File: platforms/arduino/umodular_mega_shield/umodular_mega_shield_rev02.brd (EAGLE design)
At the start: 53.5 x 100.1 mm, 31 parts, among them IC1 23LC1024, IC2 74HC4050/CD4050, IC3 6N138, U1 ARDUINO-MEGA-SHIELD

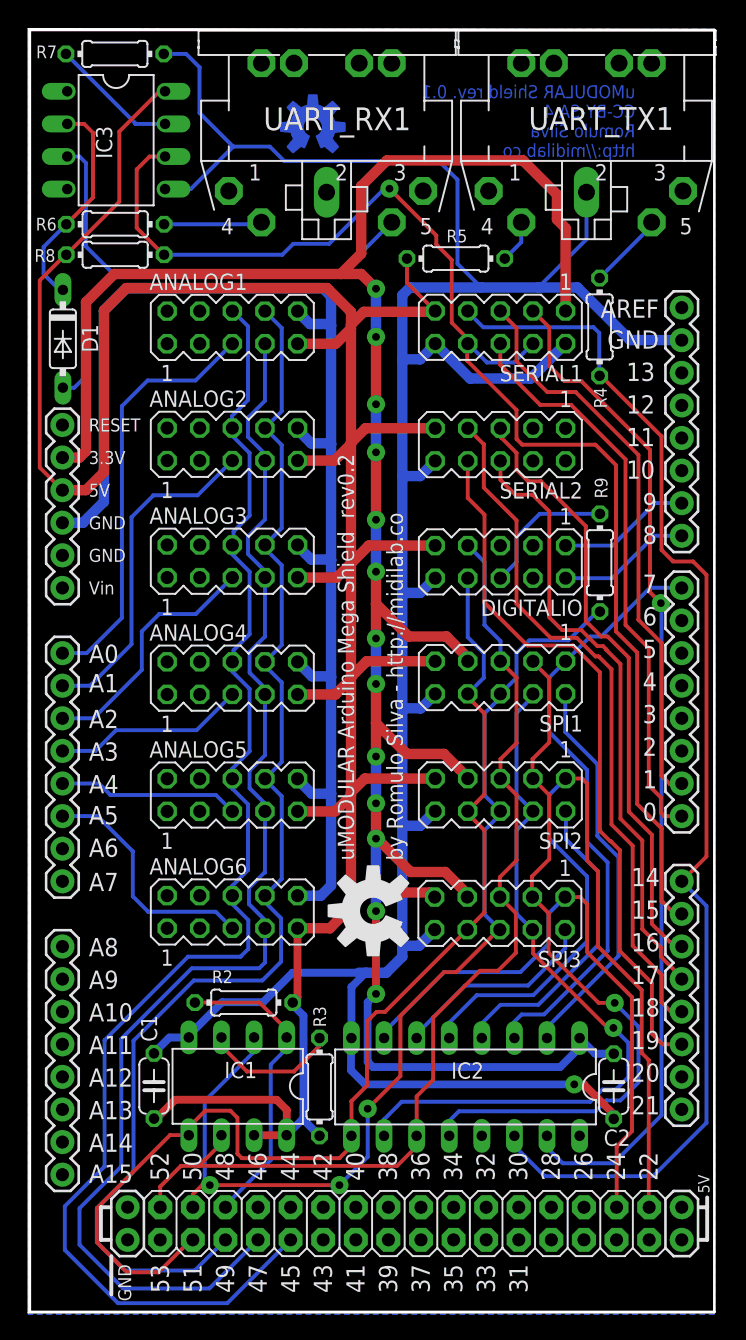
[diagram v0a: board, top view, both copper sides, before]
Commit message: added platform arduino mega shiled a external power connector.
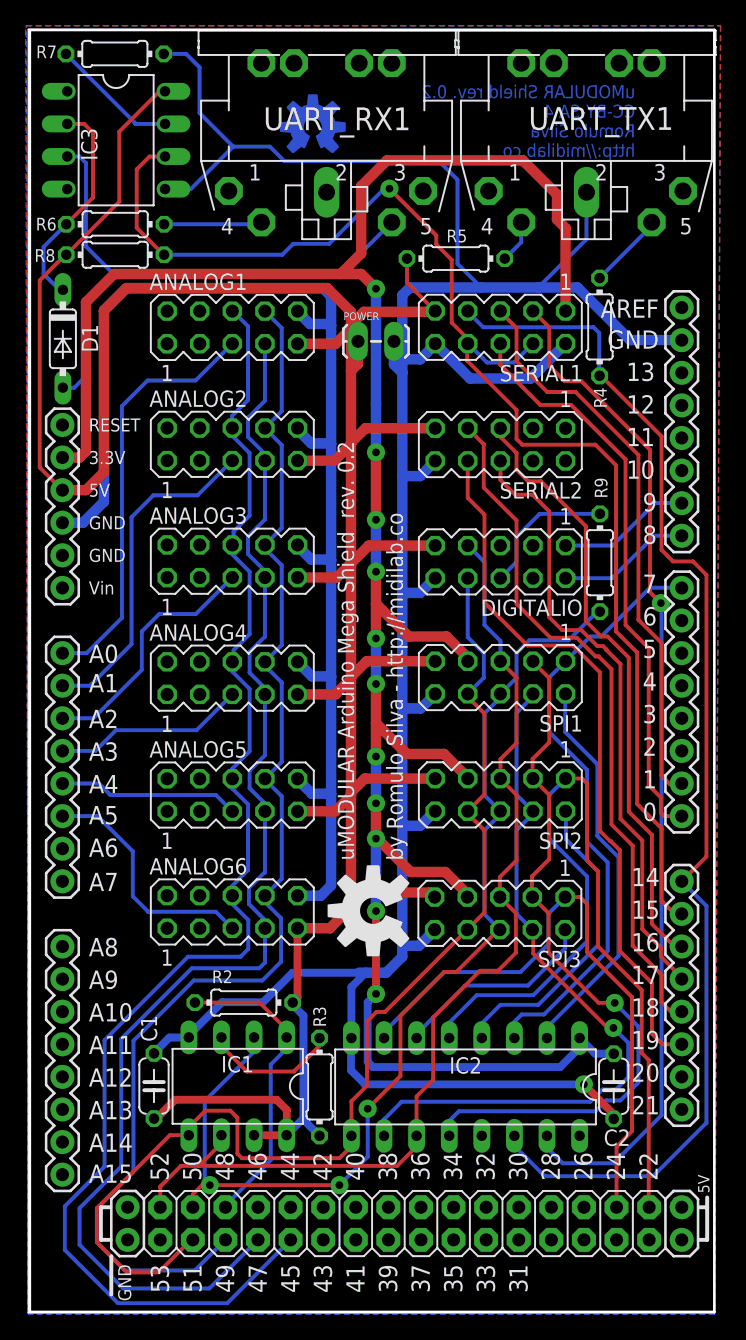
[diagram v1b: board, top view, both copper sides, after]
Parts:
- added POWER: +5V, SparkFun-Connectors:1X02_LOCK_LONGPADS
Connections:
- net GND: now also POWER.2
- net VCC: now also POWER.1
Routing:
- net GND: track 213.0 -> 215.7 mm
- net VCC: track 230.1 -> 232.6 mm
- net VCC_3_3V: vias 13 -> 11
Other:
- board size 53.5 x 100.1 mm -> 53.5 x 100 mm
- board text added: "uMODULAR Arduino Mega Shield rev. 0.2 by Romulo Silva - http://midilab.co"
- board text added: "uMODULAR Shield rev. 0.2 CC-BY-SA 4 Romulo Silva http://midilab.co"
- board text removed: "uMODULAR Arduino Mega Shield rev0.2 by Romulo Silva - http://midilab.co"
- board text removed: "uMODULAR Shield rev. 0.1 CC-BY-SA 4 Romulo Silva http://midilab.co"
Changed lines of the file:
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@@
 <setting verticaltext="up"/>
 </settings>
-<grid distance="0.05" unitdist="mm" unit="mm" style="lines" multiple="1" display="yes" altdistance="0.25" altunitdist="inch" altunit="inch"/>
+<grid distance="0.01" unitdist="mm" unit="mm" style="lines" multiple="1" display="yes" altdistance="0.25" altunitdist="inch" altunit="inch"/>
 <layers>
 <layer number="1" name="Top" color="4" fill="1" visible="yes" active="yes"/>
@@
 <wire x1="0" y1="0" x2="53.465" y2="0" width="0" layer="20"/>
 <wire x1="53.465" y1="0" x2="53.465" y2="100" width="0" layer="20"/>
-<wire x1="53.465" y1="100" x2="0" y2="100.07" width="0" layer="20"/>
-<wire x1="0" y1="100.07" x2="0" y2="0" width="0" layer="20"/>
-<text x="47.3" y="90.075" size="1.016" layer="16" font="vector" rot="MR0">uMODULAR Shield rev. 0.1
+<wire x1="53.465" y1="100" x2="0" y2="100.02" width="0" layer="20"/>
+<wire x1="0" y1="100.02" x2="0" y2="0" width="0" layer="20"/>
+<text x="47.3" y="90.075" size="1.016" layer="16" font="vector" rot="MR0">uMODULAR Shield rev. 0.2
 CC-BY-SA 4
 Romulo Silva
 http://midilab.co</text>
-<text x="29.2" y="35.25" size="1.27" layer="25" rot="R90">uMODULAR Arduino Mega Shield  rev0.2
+<text x="29.2" y="35.25" size="1.27" layer="25" rot="R90">uMODULAR Arduino Mega Shield  rev. 0.2
 by Romulo Silva - http://midilab.co</text>
 </plain>
@@
 <element name="U$1" library="SparkFun-Aesthetics3" package="OSHW-LOGO-M" value="" x="22.175" y="92.4" smashed="yes"/>
 <element name="IC1" library="ic-package" package="DIL08" value="23LC1024" x="16.325" y="17.65" smashed="yes" rot="R180">
-<attribute name="NAME" x="15.279" y="18.284" size="1.27" layer="25" ratio="10"/>
-<attribute name="VALUE" x="21.031" y="16.985" size="1.27" layer="27" ratio="10" rot="R180"/>
+<attribute name="NAME" x="15.029" y="18.734" size="1.27" layer="25" ratio="10"/>
+<attribute name="VALUE" x="21.081" y="18.235" size="1.27" layer="27" ratio="10" rot="R180"/>
 </element>
 <element name="R2" library="rcl" package="0204/7@1" value="10k" x="16.8" y="24.175" smashed="yes" rot="R180">
@@
 <attribute name="MF" value="VISHAY/TELEFUNKEN" x="0.6" y="124" size="1.778" layer="27" rot="R270" display="off"/>
 <attribute name="OC_FARNELL" value="9860150" x="0.6" y="124" size="1.778" layer="27" rot="R270" display="off"/>
-<attribute name="NAME" x="6.541" y="89.929" size="1.27" layer="25" ratio="10" rot="R90"/>
-<attribute name="VALUE" x="7.465" y="93.831" size="1.27" layer="27" ratio="10" rot="R270"/>
+<attribute name="NAME" x="5.391" y="89.779" size="1.27" layer="25" ratio="10" rot="R90"/>
+<attribute name="VALUE" x="6.215" y="93.831" size="1.27" layer="27" ratio="10" rot="R270"/>
 </element>
 <element name="R4" library="rcl" package="0204/7@1" value="220" x="44.525" y="76.825" smashed="yes" rot="R90">
@@
 </element>
 <element name="IC2" library="ic-package" package="DIL16" value="74HC4050/CD4050" x="34.075" y="17.6" smashed="yes" rot="R180">
-<attribute name="NAME" x="32.954" y="18.241" size="1.27" layer="25" ratio="10"/>
-<attribute name="VALUE" x="42.718" y="17.035" size="1.27" layer="27" ratio="10" rot="R180"/>
+<attribute name="NAME" x="32.804" y="18.641" size="1.27" layer="25" ratio="10"/>
+<attribute name="VALUE" x="42.718" y="18.285" size="1.27" layer="27" ratio="10" rot="R180"/>
 </element>
 <element name="C1" library="rcl" package="C050-024X044" value="100nf" x="9.8" y="17.675" smashed="yes" rot="R270">
@@
 <attribute name="NAME" x="44.1454" y="65.09" size="0.9906" layer="25" ratio="10" rot="R270"/>
 <attribute name="VALUE" x="45.0326" y="56.8244" size="0.9906" layer="27" ratio="10" rot="R90"/>
+</element>
+<element name="POWER" library="SparkFun-Connectors" package="1X02_LOCK_LONGPADS" value="+5V" x="25.83" y="75.7" smashed="yes">
+<attribute name="NAME" x="24.56" y="77.351" size="0.6096" layer="25" font="vector" ratio="20"/>
+<attribute name="VALUE" x="24.89" y="73.394" size="0.6096" layer="27" font="vector" ratio="20"/>
 </element>
 </elements>
@@
 <contactref element="C2" pad="1"/>
 <wire x1="29.15" y1="79.3" x2="29.15" y2="74.25" width="0.8128" layer="16"/>
-<wire x1="29.15" y1="74.25" x2="29.15" y2="65.2" width="0.8128" layer="16"/>
+<wire x1="29.15" y1="74.25" x2="29.15" y2="73.25" width="0.8128" layer="16"/>
+<wire x1="29.15" y1="73.25" x2="29.15" y2="65.2" width="0.8128" layer="16"/>
 <wire x1="29.15" y1="65.2" x2="29.15" y2="56.15" width="0.8128" layer="16"/>
 <wire x1="29.15" y1="56.15" x2="29.15" y2="47" width="0.8128" layer="16"/>
@@
 <wire x1="45.625" y1="15.11" x2="45.625" y2="15.475" width="0.6096" layer="1"/>
 <wire x1="45.625" y1="15.475" x2="43.3" y2="17.8" width="0.6096" layer="1"/>
-<wire x1="43.3" y1="17.8" x2="42.55" y2="17.8" width="0.6096" layer="1"/>
-<via x="42.55" y="17.8" extent="1-16" drill="0.6" diameter="1.4224"/>
-<wire x1="42.55" y1="17.8" x2="26.25" y2="17.8" width="0.6096" layer="16"/>
+<via x="43.3" y="17.8" extent="1-16" drill="0.6" diameter="1.4224"/>
+<wire x1="43.3" y1="17.8" x2="26.25" y2="17.8" width="0.6096" layer="16"/>
 <wire x1="26.25" y1="17.8" x2="25.15" y2="18.9" width="0.6096" layer="16"/>
 <wire x1="25.15" y1="18.9" x2="25.15" y2="21.375" width="0.6096" layer="16"/>
@@
 <wire x1="39.15" y1="72.8" x2="34.435" y2="72.8" width="0.8128" layer="16"/>
 <wire x1="34.435" y1="72.8" x2="31.71" y2="75.525" width="0.8128" layer="16"/>
-<wire x1="33.45" y1="88.3" x2="32.025" y2="89.725" width="0.3048" layer="16"/>
+<wire x1="33.45" y1="88.3" x2="32" y2="89.75" width="0.3048" layer="16"/>
 <wire x1="32" y1="89.75" x2="31.95" y2="89.8" width="0.3048" layer="16"/>
 <wire x1="15.975" y1="90.875" x2="13.35" y2="93.5" width="0.3048" layer="16"/>
@@
 <wire x1="18.825" y1="90.875" x2="19.95" y2="89.75" width="0.3048" layer="16"/>
 <wire x1="19.95" y1="89.75" x2="32" y2="89.75" width="0.3048" layer="16"/>
-<wire x1="32" y1="89.75" x2="32.025" y2="89.725" width="0.3048" layer="16"/>
 <polygon width="0.254" layer="16" isolate="0.6096">
-<vertex x="0" y="100"/>
-<vertex x="53.5" y="100"/>
+<vertex x="-0.15" y="100.3"/>
+<vertex x="53.95" y="100.3"/>
 <vertex x="53.5" y="-0.125"/>
 <vertex x="0" y="-0.125"/>
 </polygon>
+<contactref element="POWER" pad="2"/>
+<wire x1="28.497" y1="75.7" x2="28.497" y2="73.903" width="0.8128" layer="16"/>
+<wire x1="28.497" y1="73.903" x2="29.15" y2="73.25" width="0.8128" layer="16"/>
 </signal>
 <signal name="ANALOG_HOST_PORT_1">
@@
 <wire x1="25.15" y1="78" x2="25.15" y2="77" width="0.8128" layer="1"/>
 <wire x1="25.15" y1="77" x2="25.15" y2="76.7" width="0.8128" layer="1"/>
-<wire x1="25.15" y1="76.7" x2="25.15" y2="67.8" width="0.8128" layer="1"/>
+<wire x1="25.15" y1="76.7" x2="25.15" y2="73.4" width="0.8128" layer="1"/>
+<wire x1="25.15" y1="73.4" x2="25.15" y2="67.8" width="0.8128" layer="1"/>
 <wire x1="25.15" y1="67.8" x2="25.15" y2="67.7" width="0.8128" layer="1"/>
 <wire x1="25.15" y1="67.7" x2="25.15" y2="58.4" width="0.8128" layer="1"/>
@@
 <wire x1="26.3" y1="32.75" x2="31.315" y2="32.75" width="0.8128" layer="1"/>
 <wire x1="31.315" y1="32.75" x2="31.67" y2="32.395" width="0.8128" layer="1"/>
+<contactref element="POWER" pad="1"/>
+<wire x1="25.703" y1="75.7" x2="25.703" y2="73.953" width="0.8128" layer="1"/>
+<wire x1="25.703" y1="73.953" x2="25.15" y2="73.4" width="0.8128" layer="1"/>
 </signal>
 <signal name="ANALOG_HOST_PORT_4">
@@
 <wire x1="5.9" y1="78.1" x2="7.65" y2="79.85" width="0.8128" layer="16"/>
 <polygon width="0.3048" layer="1">
-<vertex x="53.5" y="100"/>
+<vertex x="53.95" y="100.3"/>
 <vertex x="53.5" y="0.05"/>
 <vertex x="0.05" y="0.05"/>
-<vertex x="0.1" y="100.05"/>
+<vertex x="-0.2" y="100.3"/>
 </polygon>
 </signal>
@@
 <wire x1="25.95" y1="80.95" x2="27.1" y2="79.8" width="0.8128" layer="1"/>
 <via x="27.1" y="79.8" extent="1-16" drill="0.6" diameter="1.4224"/>
-<wire x1="27.1" y1="79.8" x2="27.1" y2="76.05" width="0.8128" layer="16"/>
-<via x="27.1" y="76.05" extent="1-16" drill="0.6" diameter="1.4224"/>
-<via x="27.1" y="70.8" extent="1-16" drill="0.6" diameter="1.4224"/>
-<wire x1="27.1" y1="76.05" x2="27.1" y2="70.8" width="0.8128" layer="1"/>
-<wire x1="27.1" y1="70.8" x2="27.1" y2="67.05" width="0.8128" layer="16"/>
 <via x="27.1" y="67.05" extent="1-16" drill="0.6" diameter="1.4224"/>
 <wire x1="27.1" y1="67.05" x2="27.1" y2="61.8" width="0.8128" layer="1"/>
@@
 <wire x1="25.95" y1="87.8" x2="25.95" y2="82.55" width="0.8128" layer="1"/>
 <wire x1="25.95" y1="82.55" x2="24.35" y2="80.95" width="0.8128" layer="1"/>
+<wire x1="27.1" y1="79.8" x2="27.1" y2="70.95" width="0.8128" layer="16"/>
+<wire x1="27.1" y1="70.95" x2="27.1" y2="70.8" width="0.8128" layer="16"/>
+<wire x1="27.1" y1="67.05" x2="27.1" y2="70.8" width="0.8128" layer="16"/>
 </signal>
 <signal name="SPI_SS1_3_3V">
